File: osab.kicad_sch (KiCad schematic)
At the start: 100 parts, among them CON1 TF-01A, CON2 PJ-3420-A-SMT, CON3 TYPE-C-31-M-12, Q1 BC847B, Q2 BC847B, SW1 PPP, SW10 RESET, SW11 Torch, SW2 VOL-, SW3 VOL+, SW4 CHAP-, SW5 CHAP+, SW6 OT/NT, SW7 BOOK-, SW8 BOOK+, U1 VS1000, U2 ME6211C33M5G-N, U3 CAT25640, U4 TP4055, U5 MF5853CS, U6 PAM8302AAS, Y1 12MHz

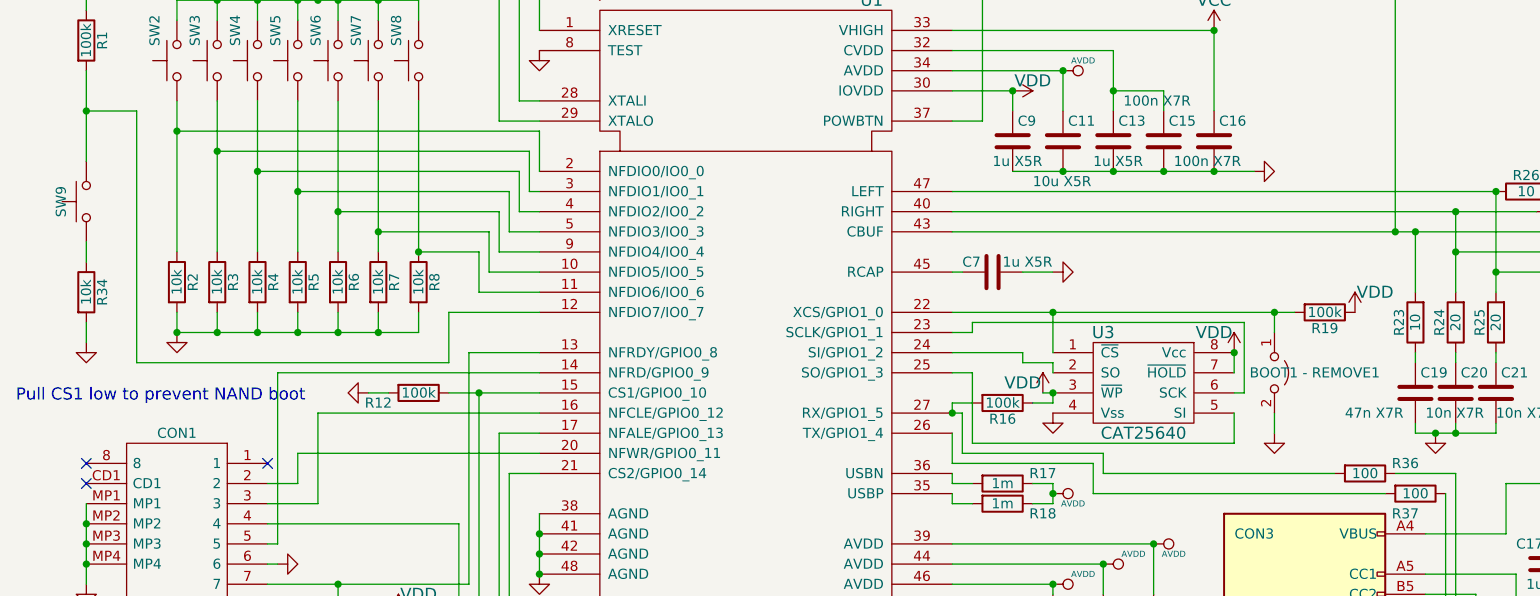
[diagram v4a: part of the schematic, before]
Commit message: production: JLCPCB board constraints + removed eeprom boot footprint
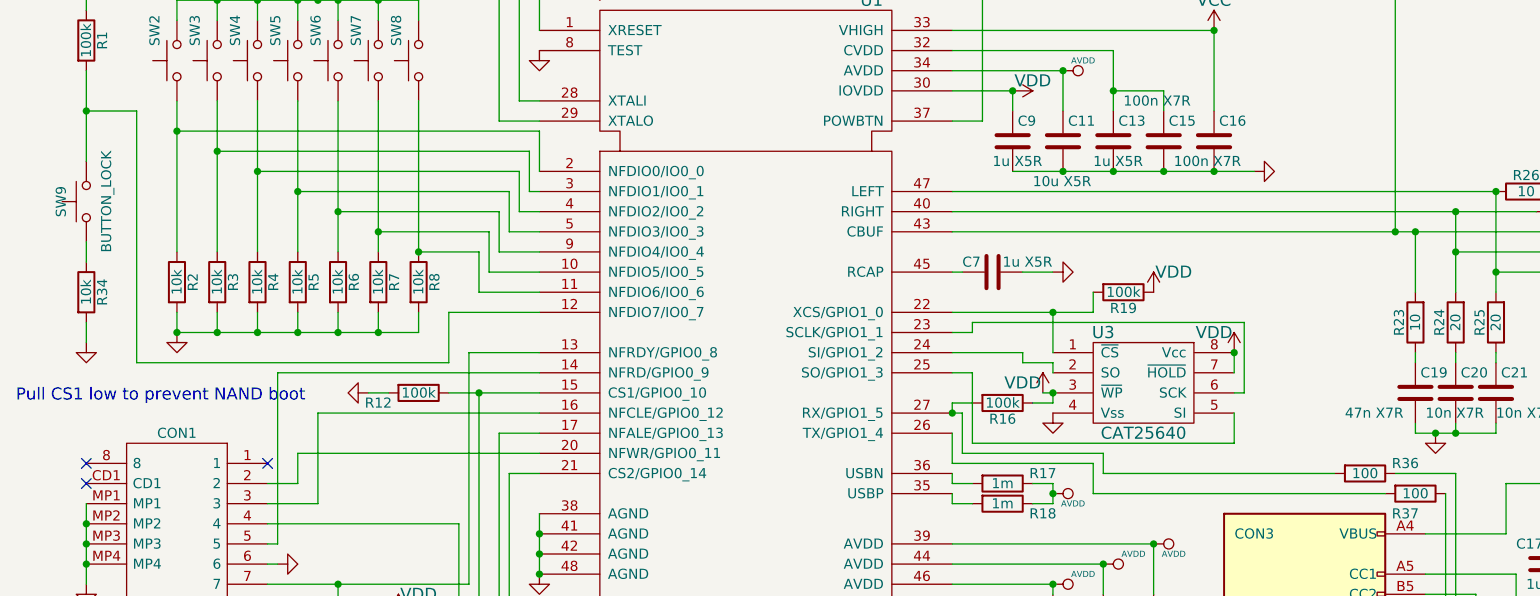
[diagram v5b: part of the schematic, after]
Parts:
- removed BOOT1 - REMOVE1: BOOT, OSAB:Terminals_2_SMD, symbol Jumper:Jumper_2_Open
- SW9: value (none) -> BUTTON_LOCK; footprint (none) -> OSAB:XKB5858-Z-F
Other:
- moved on the sheet: R19
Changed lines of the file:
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@@
   (junction (at 261.62 118.11) (diameter 0) (color 0 0 0 0)
   )
-  (junction (at 143.51 91.44) (diameter 0) (color 0 0 0 0)
-  )
   (junction (at 66.04 149.86) (diameter 0) (color 0 0 0 0)
   )
@@
   (junction (at 166.37 96.52) (diameter 0) (color 0 0 0 0)
   )
-  (junction (at 171.45 91.44) (diameter 0) (color 0 0 0 0)
-  )
   (junction (at 227.33 133.35) (diameter 0) (color 0 0 0 0)
   )
@@
   (junction (at 58.42 52.07) (diameter 0) (color 0 0 0 0)
   )
+  (junction (at 143.51 91.44) (diameter 0) (color 0 0 0 0)
+  )
   (junction (at 243.84 99.06) (diameter 0) (color 0 0 0 0)
   )
@@
     (stroke (width 0) (type default) (color 0 0 0 0))
   )
-  (wire (pts (xy 171.45 93.98) (xy 171.45 91.44))
-    (stroke (width 0) (type default) (color 0 0 0 0))
-  )
   (wire (pts (xy 130.81 114.3) (xy 130.81 115.57))
     (stroke (width 0) (type default) (color 0 0 0 0))
@@
     (stroke (width 0) (type default) (color 0 0 0 0))
   )
+  (wire (pts (xy 143.51 91.44) (xy 148.59 91.44))
+    (stroke (width 0) (type default) (color 0 0 0 0))
+  )
   (wire (pts (xy 264.16 120.65) (xy 264.16 121.92))
     (stroke (width 0) (type default) (color 0 0 0 0))
@@
     (stroke (width 0) (type default) (color 0 0 0 0))
   )
-  (wire (pts (xy 171.45 104.14) (xy 171.45 106.68))
-    (stroke (width 0) (type default) (color 0 0 0 0))
-  )
   (wire (pts (xy 193.04 138.43) (xy 190.5 138.43))
     (stroke (width 0) (type default) (color 0 0 0 0))
@@
     (stroke (width 0) (type default) (color 0 0 0 0))
   )
+  (wire (pts (xy 148.59 91.44) (xy 148.59 88.9))
+    (stroke (width 0) (type default) (color 0 0 0 0))
+  )
   (wire (pts (xy 31.75 149.86) (xy 39.37 149.86))
     (stroke (width 0) (type default) (color 0 0 0 0))
@@
     (stroke (width 0) (type default) (color 0 0 0 0))
   )
-  (wire (pts (xy 171.45 91.44) (xy 173.99 91.44))
-    (stroke (width 0) (type default) (color 0 0 0 0))
-  )
   (wire (pts (xy 50.8 104.14) (xy 50.8 115.57))
     (stroke (width 0) (type default) (color 0 0 0 0))
@@
     (stroke (width 0) (type default) (color 0 0 0 0))
   )
-  (wire (pts (xy 143.51 91.44) (xy 171.45 91.44))
-    (stroke (width 0) (type default) (color 0 0 0 0))
-  )
   (wire (pts (xy 215.9 54.61) (xy 215.9 57.15))
     (stroke (width 0) (type default) (color 0 0 0 0))
@@
     (pin "1")
   )
-  (symbol (lib_id "Jumper:Jumper_2_Open") (at 171.45 99.06 270) (unit 1)
-    (in_bom yes) (on_board yes)
-    (property "Reference" "BOOT1 - REMOVE1" (id 0) (at 176.53 99.06 90))
-    (property "Value" "BOOT" (id 1) (at 169.418 99.06 0)
-      (effects (font (size 1.27 1.27)) hide)
-    )
-    (property "Footprint" "OSAB:Terminals_2_SMD" (id 2) (at 171.45 99.06 0)
-      (effects (font (size 1.524 1.524)) hide)
-    )
-    (property "Datasheet" "https://datasheet.lcsc.com/szlcsc/1912111437_MINTRON-MTP125-1102S1_C358684.pdf" (id 3) (at 171.45 99.06 0)
-      (effects (font (size 1.524 1.524)) hide)
-    )
-    (property "3D-model" "Included in KiCad" (id 4) (at 171.45 99.06 0)
-      (effects (font (size 1.27 1.27)) hide)
-    )
-    (property "Link" "https://lcsc.com/product-detail/Pin-Header-Female-Header_MINTRON-MTP125-1102S1_C358684.html" (id 5) (at 171.45 99.06 0)
-      (effects (font (size 1.27 1.27)) hide)
-    )
-    (property "MPN" "MTP125-1102S1" (id 6) (at 171.45 99.06 0)
-      (effects (font (size 1.27 1.27)) hide)
-    )
-    (pin "1")
-    (pin "2")
-  )
-  (symbol (lib_id "power:GND") (at 171.45 106.68 0) (unit 1)
-    (in_bom yes) (on_board yes)
-    (property "Reference" "#PWR038" (id 0) (at 171.45 113.03 0)
-      (effects (font (size 1.524 1.524)) hide)
-    )
-    (property "Value" "GND" (id 1) (at 171.45 110.49 0)
-      (effects (font (size 1.524 1.524)) hide)
-    )
-    (property "Footprint" "" (id 2) (at 171.45 106.68 0)
-      (effects (font (size 1.524 1.524)))
-    )
-    (property "Datasheet" "" (id 3) (at 171.45 106.68 0)
-      (effects (font (size 1.524 1.524)))
-    )
-    (pin "1")
-  )
-  (symbol (lib_id "power:VDD") (at 181.61 91.44 0) (unit 1)
+  (symbol (lib_id "power:VDD") (at 156.21 88.9 0) (unit 1)
     (in_bom yes) (on_board yes)
-    (property "Reference" "#PWR039" (id 0) (at 181.61 95.25 0)
+    (property "Reference" "#PWR039" (id 0) (at 156.21 92.71 0)
       (effects (font (size 1.524 1.524)) hide)
     )
-    (property "Value" "VDD" (id 1) (at 184.15 88.9 0)
+    (property "Value" "VDD" (id 1) (at 158.75 86.36 0)
       (effects (font (size 1.524 1.524)))
     )
-    (property "Footprint" "" (id 2) (at 181.61 91.44 0)
+    (property "Footprint" "" (id 2) (at 156.21 88.9 0)
       (effects (font (size 1.524 1.524)))
     )
-    (property "Datasheet" "" (id 3) (at 181.61 91.44 0)
+    (property "Datasheet" "" (id 3) (at 156.21 88.9 0)
       (effects (font (size 1.524 1.524)))
     )
@@
     (pin "2")
   )
-  (symbol (lib_id "Device:R") (at 177.8 91.44 270) (unit 1)
+  (symbol (lib_id "Device:R") (at 152.4 88.9 270) (unit 1)
     (in_bom yes) (on_board yes)
-    (property "Reference" "R19" (id 0) (at 177.8 93.472 90))
-    (property "Value" "100k" (id 1) (at 177.8 91.44 90))
-    (property "Footprint" "Resistor_SMD:R_0603_1608Metric" (id 2) (at 177.8 89.662 90)
+    (property "Reference" "R19" (id 0) (at 152.4 90.932 90))
+    (property "Value" "100k" (id 1) (at 152.4 88.9 90))
+    (property "Footprint" "Resistor_SMD:R_0603_1608Metric" (id 2) (at 152.4 87.122 90)
       (effects (font (size 1.27 1.27)) hide)
     )
-    (property "Datasheet" "https://datasheet.lcsc.com/lcsc/1811091512_Viking-Tech-ARG03FTC1003_C217682.pdf" (id 3) (at 177.8 91.44 0)
+    (property "Datasheet" "https://datasheet.lcsc.com/lcsc/1811091512_Viking-Tech-ARG03FTC1003_C217682.pdf" (id 3) (at 152.4 88.9 0)
       (effects (font (size 1.27 1.27)) hide)
     )
-    (property "3D-model" "Included in KiCad" (id 4) (at 177.8 91.44 0)
+    (property "3D-model" "Included in KiCad" (id 4) (at 152.4 88.9 0)
       (effects (font (size 1.27 1.27)) hide)
     )
-    (property "Link" "https://lcsc.com/product-detail/Chip-Resistor-Surface-Mount_Viking-Tech-ARG03FTC1003_C217682.html" (id 5) (at 177.8 91.44 0)
+    (property "Link" "https://lcsc.com/product-detail/Chip-Resistor-Surface-Mount_Viking-Tech-ARG03FTC1003_C217682.html" (id 5) (at 152.4 88.9 0)
       (effects (font (size 1.27 1.27)) hide)
     )
-    (property "MPN" "ARG03FTC1003" (id 6) (at 177.8 91.44 0)
+    (property "MPN" "ARG03FTC1003" (id 6) (at 152.4 88.9 0)
       (effects (font (size 1.27 1.27)) hide)
     )
@@
     (in_bom yes) (on_board yes)
     (property "Reference" "SW9" (id 0) (at 18.415 77.47 0))
-    (property "Value" "" (id 1) (at 24.13 77.47 0))
-    (property "Footprint" "" (id 2) (at 21.59 77.47 0)
+    (property "Value" "BUTTON_LOCK" (id 1) (at 24.13 77.47 0))
+    (property "Footprint" "OSAB:XKB5858-Z-F" (id 2) (at 21.59 77.47 0)
       (effects (font (size 1.27 1.27)) hide)
     )
@@
       (reference "#PWR037") (unit 1) (value "GND") (footprint "")
     )
-    (path "/00000000-0000-0000-0000-000054d41e8f"
-      (reference "#PWR038") (unit 1) (value "GND") (footprint "")
-    )
     (path "/00000000-0000-0000-0000-000054d422bd"
       (reference "#PWR039") (unit 1) (value "VDD") (footprint "")
@@
       (reference "BATTERY2") (unit 1) (value "Conn_01x02") (footprint "Connector_JST:JST_PH_B2B-PH-SM4-TB_1x02-1MP_P2.00mm_Vertical")
     )
-    (path "/00000000-0000-0000-0000-000054d41aff"
-      (reference "BOOT1 - REMOVE1") (unit 1) (value "BOOT") (footprint "OSAB:Terminals_2_SMD")
-    )
     (path "/00000000-0000-0000-0000-00005e12db10"

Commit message: production: 50 mm wide PCB before laying traces
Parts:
- removed BATTERY2: Conn_01x02, Connector_JST:JST_PH_B2B-PH-SM4-TB_1x02-1MP_P2.00mm_Vertical, symbol Connector_Generic:Conn_01x02
- removed BT2: BATTERY, OSAB:NULL, symbol osab:BATTERY
- removed SW9: BUTTON_LOCK, OSAB:XKB5858-Z-F, symbol Switch:SW_Push
- added SW9: XKB5858-Z-F, OSAB:XKB5858-Z-F, symbol osab:XKB5858-Z-F
- BATTERY1: footprint Connector_JST:JST_PH_B2B-PH-SM4-TB_1x02-1MP_P2.00mm_Vertical -> Connector_JST:JST_PH_S2B-PH-SM4-TB_1x02-1MP_P2.00mm_Horizontal; Link https://lcsc.com/product-detail/Wire-To-Board-Wire-To-Wire-Connector_Shenzhen-Kinghelm-Elec-KH-A2001LF-2A_C2898963.html -> https://lcsc.com/product-detail/Wire-To-Board-Wire-To-Wire-Connector_Shenzhen-Kinghelm-Elec-KH-A2001WF-02A_C2688784.html; MPN KH-A2001LF-2A -> KH-A2001WF-02A
- BT1: value BATTERY -> Lipo battery; Link (none) -> http://www.benzoenergy.com/china-li-ion-battery-manufacture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; MPN (none) -> BZ 602030
- CON3: value TYPE-C-31-M-12 -> (none); footprint Connector_USB:USB_C_Receptacle_HRO_TYPE-C-31-M-12 -> (none)
- D1: footprint LED_SMD:LED_0603_1608Metric -> OSAB:0602-LED; 3D-model NOT Included in KiCad -> (none)
- D2: footprint LED_SMD:LED_0603_1608Metric -> OSAB:0602-LED
- SPEAKER1: footprint Connector_JST:JST_SH_BM02B-SRSS-TB_1x02-1MP_P1.00mm_Vertical -> Connector_JST:JST_SH_SM02B-SRSS-TB_1x02-1MP_P1.00mm_Horizontal; Link https://lcsc.com/product-detail/Wire-To-Board-Wire-To-Wire-Connector_Shenzhen-Kinghelm-Elec-KH-A1001LF-02A_C2688754.html -> https://lcsc.com/product-detail/Wire-To-Board-Wire-To-Wire-Connector_Shenzhen-Kinghelm-Elec-KH-A1001WF-02A_C2688759.html; MPN KH-A1001LF-02A -> KH-A1001WF-02A
- SW1, SW10, SW11, SW2, SW3, SW4, SW5, SW6, SW7, SW8: footprint Button_Switch_SMD:SW_SPST_TL3342 -> OSAB:SW_SPST_TL3342
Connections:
- net at R1.2, U1.12 (NFDIO7/IO0_7): now also SW9.4, SW9.6
- net at R34.1: now also SW9.2, SW9.5
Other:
- note added: "Button lock"
- note removed: "4.5V alkaline battery"
- moved on the sheet: R16

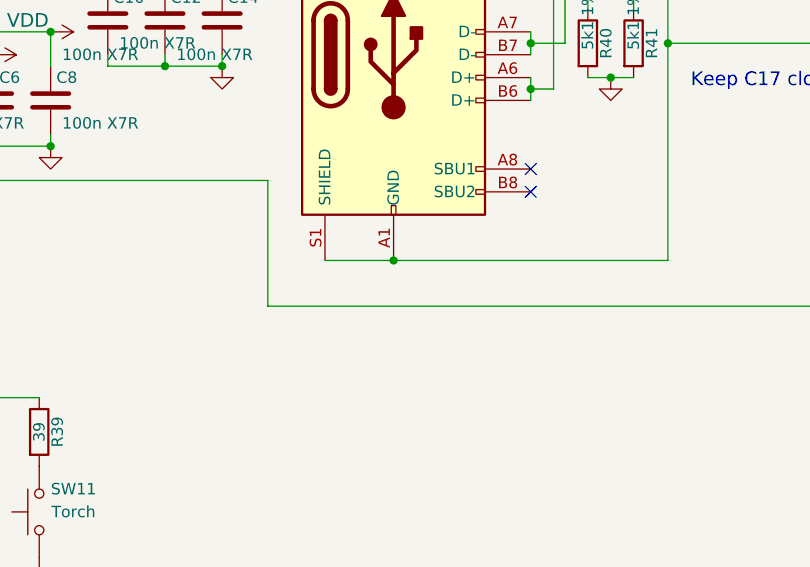
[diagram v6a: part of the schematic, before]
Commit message: production: Changed speaker + conn for speaker; Added GND plane splits for GNDA
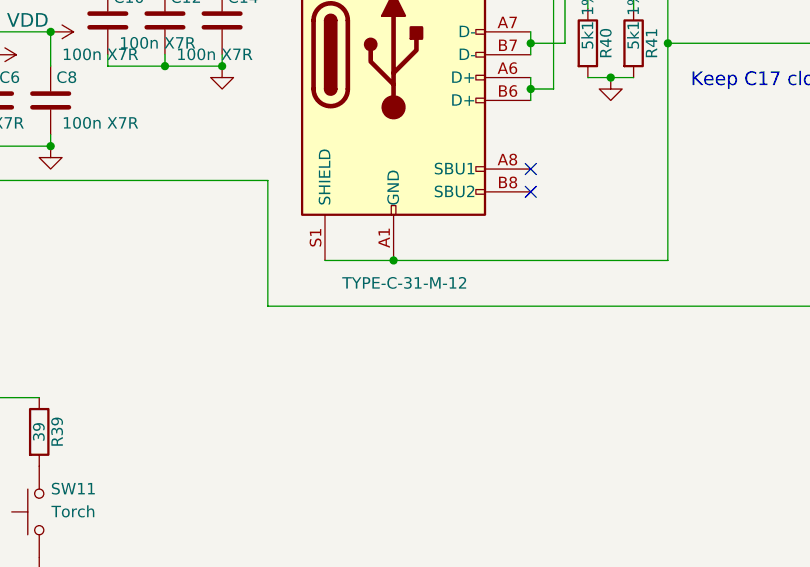
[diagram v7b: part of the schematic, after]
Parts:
- CON3: value (none) -> TYPE-C-31-M-12; footprint (none) -> OSAB:USB_C_Receptacle_HRO_TYPE-C-31-M-12
- SP1: LCSC (none) -> C391017; Link https://lcsc.com/product-detail/Speakers_FUET-30M01-8T-H49_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 -> https://lcsc.com/product-detail/Speakers_FUET-28M03-8T-H52-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; MPN 30M01-8T-H49 -> 28M03-8T-H52-L70
- SPEAKER1: footprint Connector_JST:JST_SH_SM02B-SRSS-TB_1x02-1MP_P1.00mm_Horizontal -> Connector_JST:JST_GH_SM02B-GHS-TB_1x02-1MP_P1.25mm_Horizontal; LCSC (none) -> C2939022; Link https://lcsc.com/product-detail/Wire-To-Board-Wire-To-Wire-Connector_Shenzhen-Kinghelm-Elec-KH-A1001WF-02A_C2688759.html -> https://lcsc.com/product-detail/Wire-To-Board-Wire-To-Wire-Connector_HOAUC-HYCW02-WF02-125B_C2939022.html; MPN KH-A1001WF-02A -> HYCW02-WF02-125B
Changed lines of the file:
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@@
   (title_block
     (title "OSAB - the Open Source Audio Bible player")
-    (date "2022-04-20")
+    (date "2022-05-18")
     (rev "7")
     (company "theaudiobible.org")
@@
     (in_bom yes) (on_board yes)
     (property "Reference" "CON3" (id 0) (at 168.91 119.38 0))
-    (property "Value" "" (id 1) (at 176.53 160.02 0))
-    (property "Footprint" "" (id 2) (at 179.07 134.62 0)
+    (property "Value" "TYPE-C-31-M-12" (id 1) (at 176.53 160.02 0))
+    (property "Footprint" "OSAB:USB_C_Receptacle_HRO_TYPE-C-31-M-12" (id 2) (at 179.07 134.62 0)
       (effects (font (size 1.27 1.27)) hide)
     )
@@
       (effects (font (size 1.27 1.27)) (justify left) hide)
     )
-    (property "Footprint" "Connector_JST:JST_SH_SM02B-SRSS-TB_1x02-1MP_P1.00mm_Horizontal" (id 2) (at 276.86 78.74 0)
+    (property "Footprint" "Connector_JST:JST_GH_SM02B-GHS-TB_1x02-1MP_P1.25mm_Horizontal" (id 2) (at 276.86 78.74 0)
       (effects (font (size 1.27 1.27)) hide)
     )
-    (property "Datasheet" "https://datasheet.lcsc.com/lcsc/2106070036_Shenzhen-Kinghelm-Elec-KH-A1001WF-02A_C2688759.pdf" (id 3) (at 276.86 78.74 0)
+    (property "Datasheet" "https://datasheet.lcsc.com/lcsc/2201261500_HOAUC-HYCW02-WF02-125B_C2939022.pdf" (id 3) (at 276.86 78.74 0)
       (effects (font (size 1.27 1.27)) hide)
     )
-    (property "Link" "https://lcsc.com/product-detail/Wire-To-Board-Wire-To-Wire-Connector_Shenzhen-Kinghelm-Elec-KH-A1001WF-02A_C2688759.html" (id 5) (at 276.86 78.74 0)
+    (property "Link" "https://lcsc.com/product-detail/Wire-To-Board-Wire-To-Wire-Connector_HOAUC-HYCW02-WF02-125B_C2939022.html" (id 5) (at 276.86 78.74 0)
       (effects (font (size 1.27 1.27)) hide)
     )
-    (property "MPN" "KH-A1001WF-02A" (id 6) (at 276.86 78.74 0)
+    (property "MPN" "HYCW02-WF02-125B" (id 6) (at 276.86 78.74 0)
       (effects (font (size 1.27 1.27)) hide)
     )
+    (property "LCSC" "C2939022" (id 7) (at 276.86 78.74 0)
+      (effects (font (size 1.524 1.524)) hide)
+    )
     (pin "1")
     (pin "2")
@@
       (effects (font (size 1.524 1.524)) hide)
     )
-    (property "Datasheet" "https://datasheet.lcsc.com/lcsc/1912111437_FUET-30M01-8T-H49_C391018.pdf" (id 3) (at 280.67 74.93 0)
+    (property "Datasheet" "https://datasheet.lcsc.com/lcsc/2102031904_FUET-28M03-8T-H52-L70_C391017.pdf" (id 3) (at 280.67 74.93 0)
       (effects (font (size 1.524 1.524)) hide)
     )
-    (property "Link" "https://lcsc.com/product-detail/Speakers_FUET-30M01-8T-H49_C391018.html" (id 4) (at 280.67 74.93 0)
+    (property "Link" "https://lcsc.com/product-detail/Speakers_FUET-28M03-8T-H52-L70_C391017.html" (id 4) (at 280.67 74.93 0)
       (effects (font (size 1.27 1.27)) hide)
     )
-    (property "MPN" "30M01-8T-H49" (id 5) (at 280.67 74.93 0)
+    (property "MPN" "28M03-8T-H52-L70" (id 5) (at 280.67 74.93 0)
       (effects (font (size 1.27 1.27)) hide)
     )
+    (property "LCSC" "C391017" (id 7) (at 280.67 74.93 0)
+      (effects (font (size 1.524 1.524)) hide)
+    )
   )
   (symbol (lib_id "osab:BATTERY") (at 274.32 115.57 0) (unit 1)
@@
     )
     (path "/00000000-0000-0000-0000-00005e03f86a"
-      (reference "SPEAKER1") (unit 1) (value "Conn_01x02") (footprint "Connector_JST:JST_SH_SM02B-SRSS-TB_1x02-1MP_P1.00mm_Horizontal")
+      (reference "SPEAKER1") (unit 1) (value "Conn_01x02") (footprint "Connector_JST:JST_GH_SM02B-GHS-TB_1x02-1MP_P1.25mm_Horizontal")
     )
     (path "/00000000-0000-0000-0000-0000543f883c"

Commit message: production: Routed analog tracks
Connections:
- net GNDA is gone; now on net GND: U1.38 (AGND), U1.41 (AGND), U1.42 (AGND), U1.48 (AGND)
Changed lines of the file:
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@@
   (title_block
     (title "OSAB - the Open Source Audio Bible player")
-    (date "2022-05-18")
+    (date "2022-05-30")
     (rev "7")
     (company "theaudiobible.org")
@@
     (stroke (width 0) (type default) (color 0 0 0 0))
   )
+  (wire (pts (xy 78.74 124.46) (xy 76.2 124.46))
+    (stroke (width 0) (type default) (color 0 0 0 0))
+  )
   (wire (pts (xy 78.74 129.54) (xy 78.74 132.08))
     (stroke (width 0) (type default) (color 0 0 0 0))
@@
     (stroke (width 0) (type default) (color 0 0 0 0))
   )
+  (wire (pts (xy 76.2 132.08) (xy 78.74 132.08))
+    (stroke (width 0) (type default) (color 0 0 0 0))
+  )
   (wire (pts (xy 39.37 149.86) (xy 41.91 149.86))
     (stroke (width 0) (type default) (color 0 0 0 0))
@@
   )
   (wire (pts (xy 241.3 101.6) (xy 241.3 107.95))
+    (stroke (width 0) (type default) (color 0 0 0 0))
+  )
+  (wire (pts (xy 76.2 124.46) (xy 76.2 132.08))
     (stroke (width 0) (type default) (color 0 0 0 0))
   )
@@
       (effects (font (size 1.524 1.524)) hide)
     )
-    (property "Value" "GNDA" (id 1) (at 78.74 128.27 0)
-      (effects (font (size 1.524 1.524)))
-    )
+    (property "Value" "GNDA" (id 1) (at 82.55 127 0)
+      (effects (font (size 1.524 1.524)))
+    )
